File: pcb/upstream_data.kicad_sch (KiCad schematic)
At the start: 7 parts, among them J6 USB-C data, U12 USBLC6-2SC6

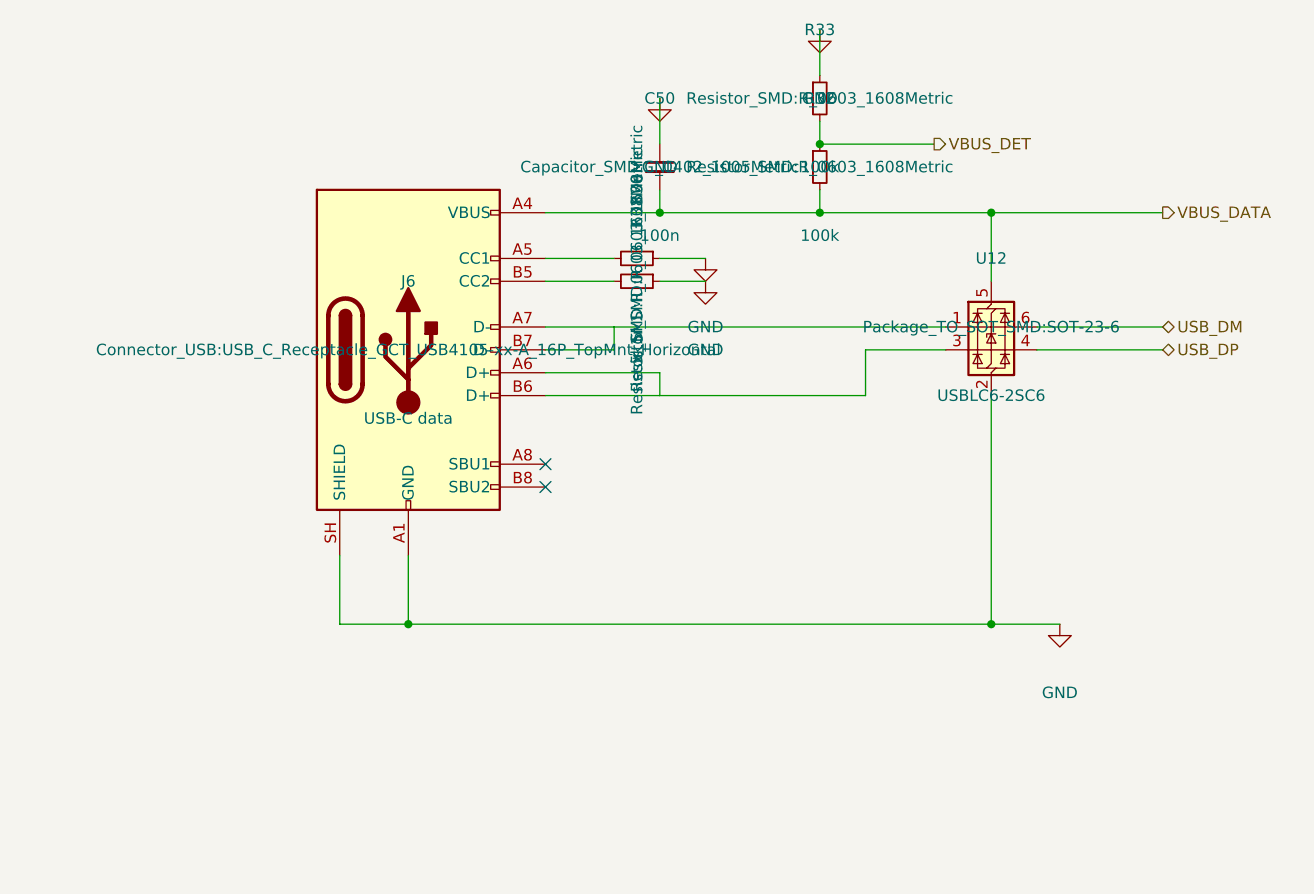
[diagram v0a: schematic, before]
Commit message: checkpoint the battery, PD and radio design as it stood
The last state of the full-featured board before it is reduced to a single
USB-C input: the power block re-placed part by part in order of importance,
the charger's signal pins fanned out, the differential pairs renamed so the
layout tool recognises them, the 3.3 V converter's feedback divider joined
to its pin, the FETs given their part number, and the non-printing fields
hidden on the schematic. The layout is incomplete and is recorded as such.

Co-Authored-By: Claude Fable 5.1 <noreply@anthropic.com>
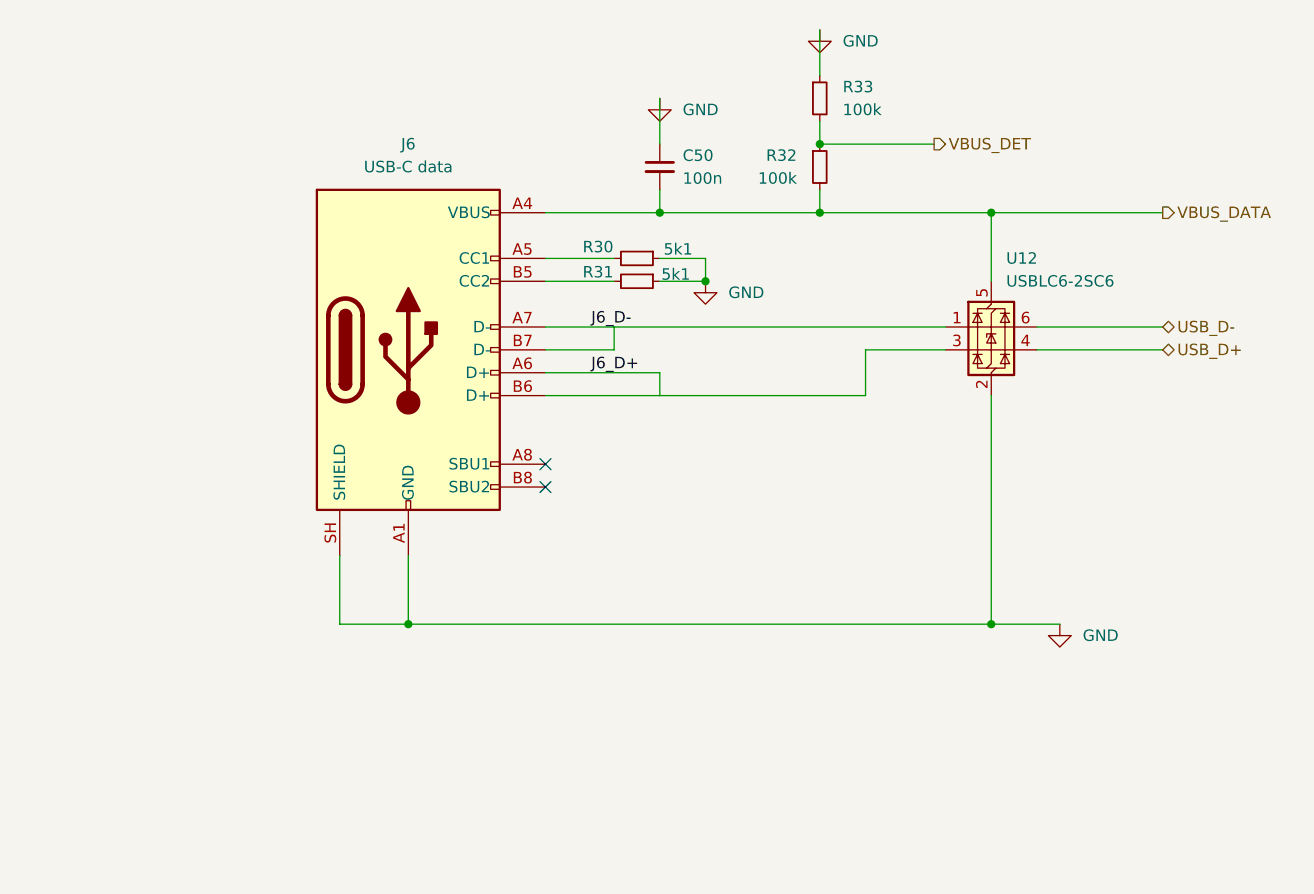
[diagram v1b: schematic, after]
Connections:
- net J6_D+: now reaches J6.A6 (D+), J6.B6 (D+), U12.3 (I/O2)
- net J6_D-: now reaches J6.A7 (D-), J6.B7 (D-), U12.1 (I/O1)
- net USB_DM renamed USB_D-
- net USB_DP renamed USB_D+

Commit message: reduce the board to a single USB-C input
The PD sink and its connector, the charger and the cell, the input and ship
switches, the 5 V boost, the 3.3 V buck-boost and the radio come off. The
one remaining USB-C receptacle carries data to the hardware controller and
its VBUS is the 5 V rail: straight to the four port switches, and to a
fixed 3.3 V buck (AP63203) for everything else.

The two CC pins are read by ADC inputs through 10k into 100n, in series so
the 5.1k termination is not loaded, so firmware can tell a 3 A source from
a 1.5 A one from a default port and power the ports to fit.

Schematic: radio and upstream_power sheets removed, power sheet redrawn,
seven MCU pins freed and two taken. Board: 61 footprints and 514 tracks and
vias removed, survivors re-netted from the netlist, new parts loaded but
not placed. The layout is to be redone and the design document says so; it
is rewritten for this design, with what the single input gives up stated.

Co-Authored-By: Claude Fable 5.1 <noreply@anthropic.com>
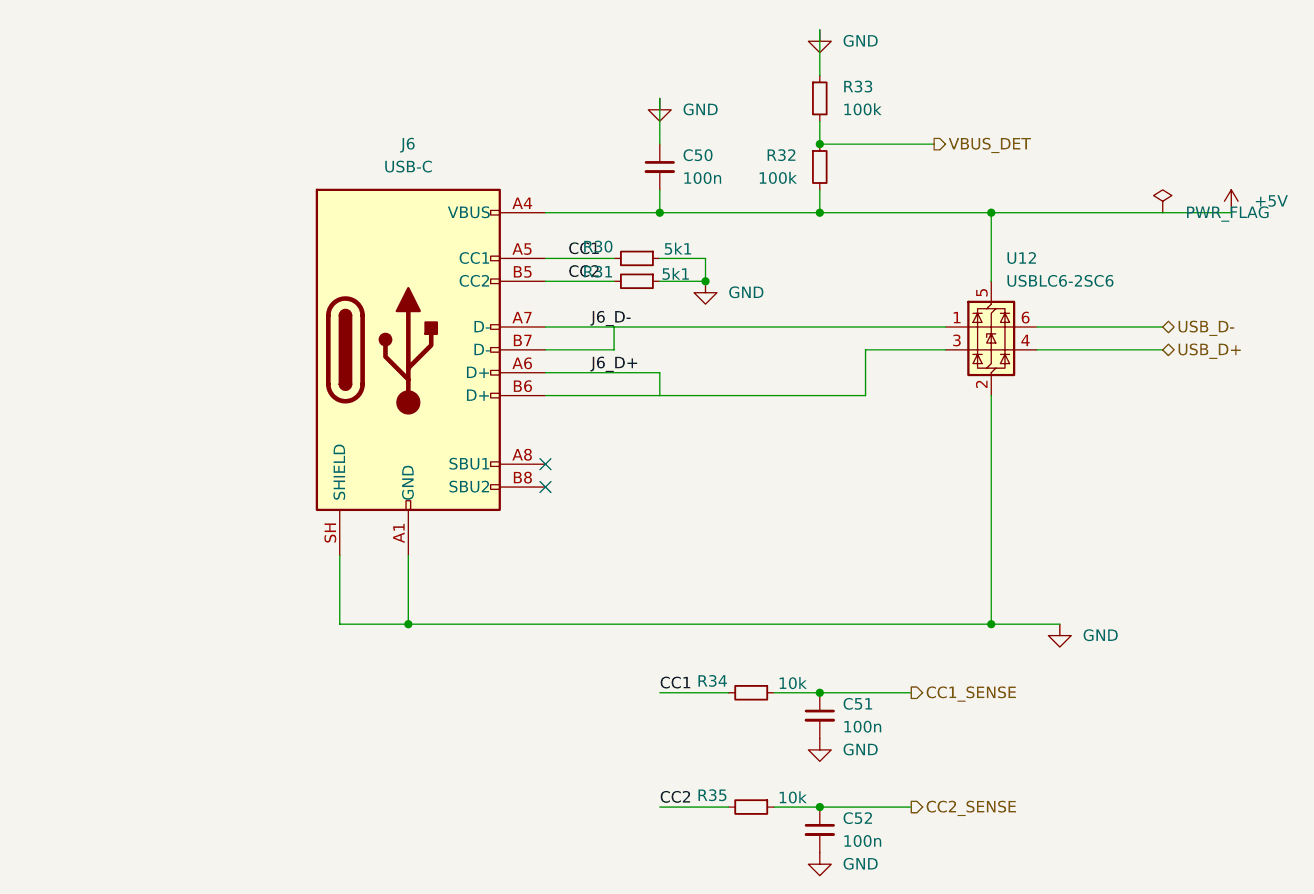
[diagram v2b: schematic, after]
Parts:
- added C51, C52: 100n, Capacitor_SMD:C_0402_1005Metric, symbol Device:C_Small
- added R34, R35: 10k, Resistor_SMD:R_0603_1608Metric, symbol Device:R_Small
- J6: value USB-C data -> USB-C
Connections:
- net GND: now also C51.2, C52.2
- net CC1: now reaches J6.A5 (CC1), R30.2
- net CC1: now also R34.2
- net CC2: now reaches J6.B5 (CC2), R31.2
- net CC2: now also R35.2
- net VBUS_DATA renamed +5V
- new net CC1_SENSE: C51.1, R34.1
- new net CC2_SENSE: C52.1, R35.1

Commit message: resistors to 0402
All nineteen, on the schematic and on the board, each keeping its identity,
position, face and nets; the placement is then rebuilt so the smaller parts
settle where they fit. The indicators stay 0603. Rules check clean; 39
items open, eighteen of them the pairs.

Co-Authored-By: Claude Fable 5.1 <noreply@anthropic.com>
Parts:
- R30, R31, R32, R33, R34, R35: footprint Resistor_SMD:R_0603_1608Metric -> Resistor_SMD:R_0402_1005Metric
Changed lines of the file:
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@@
 			)
 		)
-		(property "Footprint" "Resistor_SMD:R_0603_1608Metric"
+		(property "Footprint" "Resistor_SMD:R_0402_1005Metric"
 			(at 121.92 86.36 0)
 			(hide yes)
@@
 			)
 		)
-		(property "Footprint" "Resistor_SMD:R_0603_1608Metric"
+		(property "Footprint" "Resistor_SMD:R_0402_1005Metric"
 			(at 101.6 104.14 0)
 			(hide yes)
@@
 			)
 		)
-		(property "Footprint" "Resistor_SMD:R_0603_1608Metric"
+		(property "Footprint" "Resistor_SMD:R_0402_1005Metric"
 			(at 101.6 106.68 0)
 			(hide yes)
@@
 			)
 		)
-		(property "Footprint" "Resistor_SMD:R_0603_1608Metric"
+		(property "Footprint" "Resistor_SMD:R_0402_1005Metric"
 			(at 121.92 93.98 0)
 			(hide yes)
@@
 			)
 		)
-		(property "Footprint" "Resistor_SMD:R_0603_1608Metric"
+		(property "Footprint" "Resistor_SMD:R_0402_1005Metric"
 			(at 114.3 152.4 0)
 			(hide yes)
@@
 			)
 		)
-		(property "Footprint" "Resistor_SMD:R_0603_1608Metric"
+		(property "Footprint" "Resistor_SMD:R_0402_1005Metric"
 			(at 114.3 165.1 0)
 			(hide yes)
